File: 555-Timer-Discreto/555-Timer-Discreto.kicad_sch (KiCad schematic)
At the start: 24 parts, among them Q1 2N3904, Q10 2N3906, Q11 2N3904, Q12 2N3904, Q13 2N3906, Q14 2N3904, Q15 2N3904, Q16 2N3904, Q17 2N3904, Q18 2N3904, Q19 2N3906, Q2 2N3904, Q20 2N3906, Q21 2N3906, Q22 2N3904, Q23 2N3904, Q24 2N3904, Q3 2N3904, Q4 2N3904, Q5 2N3906, Q6 2N3906, Q7 2N3906, Q8 2N3906, Q9 2N3906

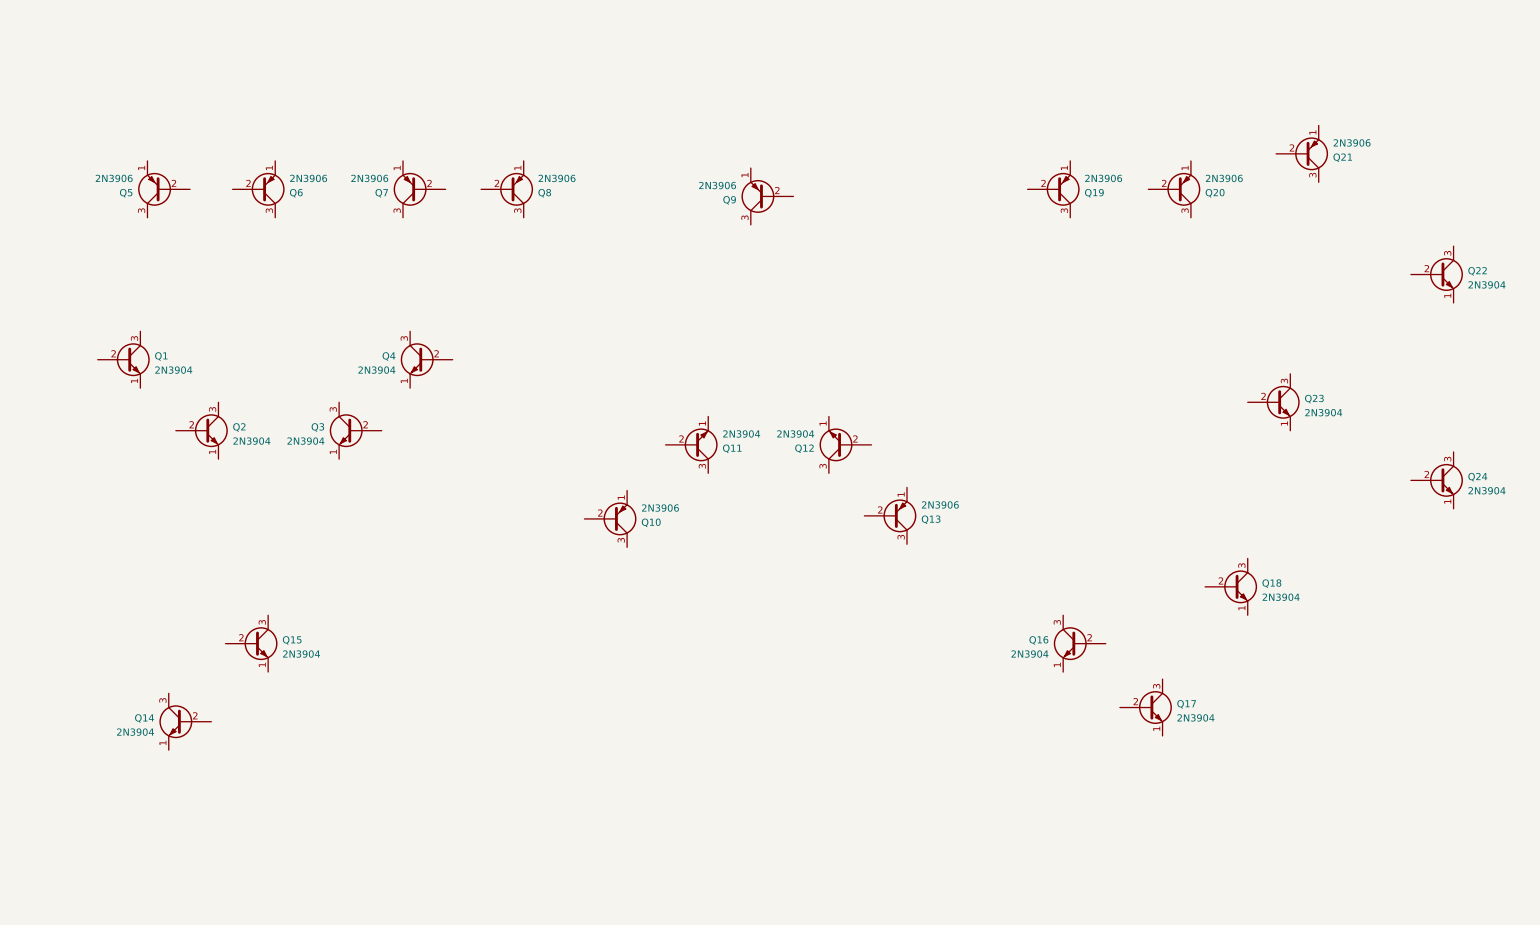
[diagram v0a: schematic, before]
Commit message: Se incorporaron el resto de los componentes y se hicieron las conexiones pertinentes
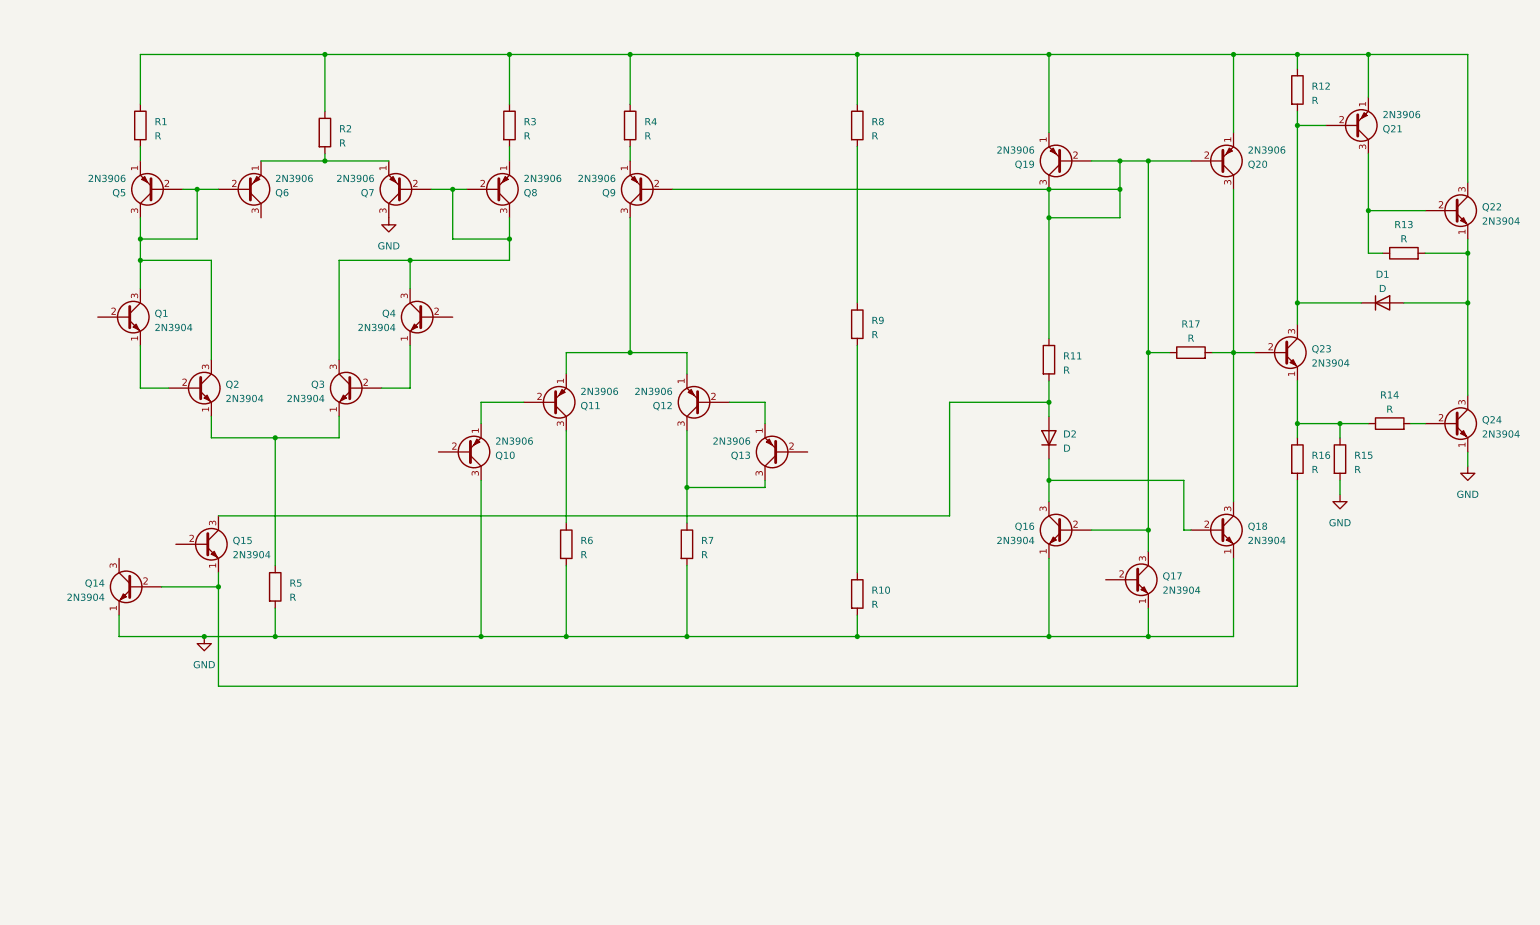
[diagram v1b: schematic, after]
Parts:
- removed Q11, Q12: 2N3904, Package_TO_SOT_THT:TO-92_Inline, symbol Transistor_BJT:2N3904
- added D1, D2: D, symbol Device:D
- added Q11, Q12: 2N3906, Package_TO_SOT_THT:TO-92_Inline, symbol Transistor_BJT:2N3906
- added R1, R10, R11, R12, R13, R14, R15, R16, R17, R2, R3, R4, R5, R6, R7, R8, R9: R, symbol Device:R
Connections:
- net GND: now reaches Q17.1 (E)
- net GND: now also Q10.3 (C), Q14.1 (E), Q16.1 (E), Q18.1 (E), Q24.1 (E), Q7.3 (C), R10.2, R15.2, R5.2, R6.2, R7.2
- net at Q17.3 (C): now also Q16.2 (B), Q19.2 (B), Q19.3 (C), Q20.2 (B), Q9.2 (B), R11.1, R17.1
- net at Q23.1 (E): now also R14.1, R15.1, R16.1
- net at Q23.2 (B): now also Q18.3 (C), Q20.3 (C), R17.2
- net at Q23.3 (C): now also Q21.2 (B), D1.1 (K), R12.2
- net at Q18.2 (B): now also Q16.3 (C), D2.1 (K)
- net at Q15.1 (E): now also Q14.2 (B), R16.2
- net at Q15.3 (C): now also D2.2 (A), R11.2
- net at Q4.1 (E): now also Q3.2 (B)
- net at Q4.3 (C): now also Q3.3 (C), Q7.2 (B), Q8.2 (B), Q8.3 (C)
- net at Q19.1 (E): now also Q20.1 (E), Q21.1 (E), Q22.3 (C), R1.1, R12.1, R2.1, R3.1, R4.1, R8.1
- net at Q10.1 (E): now also Q11.2 (B)
- net at Q9.1 (E): now also R4.2
- net at Q9.3 (C): now also Q11.1 (E), Q12.1 (E)
- net at Q1.1 (E): now also Q2.2 (B)
- net at Q1.3 (C): now also Q2.3 (C), Q5.2 (B), Q5.3 (C), Q6.2 (B)
- net at Q21.3 (C): now also Q22.2 (B), R13.1
- net at Q22.1 (E): now also Q24.3 (C), D1.2 (A), R13.2
- net at Q6.1 (E): now also Q7.1 (E), R2.2
- net at Q5.1 (E): now also R1.2
- net at Q13.1 (E): now also Q12.2 (B)
- net at Q13.3 (C): now also Q12.3 (C), R7.1
- net at Q2.1 (E): now also Q3.1 (E), R5.1
- net at Q8.1 (E): now also R3.2
- net at Q24.2 (B): now also R14.2
- new net: Q11.3 (C), R6.1
- new net: R8.2, R9.1
- new net: R10.1, R9.2
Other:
- title: (none) -> 555 TIMER
- moved on the sheet: Q1, Q10, Q13, Q14, Q15, Q16, Q17, Q18, Q19, Q2, Q20, Q21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

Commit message: Se asignaron huellas a los componentes
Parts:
- D1, D2: footprint (none) -> Diode_THT:D_A-405_P7.62mm_Horizontal
- R1, R10, R11, R12, R13, R14, R15, R16, R17, R2, R3, R4, R5, R6, R7, R8, R9: footprint (none) -> Resistor_THT:R_Axial_DIN0204_L3.6mm_D1.6mm_P5.08mm_Horizontal
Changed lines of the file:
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@@
       (effects (font (size 1.27 1.27)))
     )
-    (property "Footprint" "" (at 255.27 91.948 90)
+    (property "Footprint" "Resistor_THT:R_Axial_DIN0204_L3.6mm_D1.6mm_P5.08mm_Horizontal" (at 255.27 91.948 90)
       (effects (font (size 1.27 1.27)) hide)
     )
@@
       (effects (font (size 1.27 1.27)) (justify left))
     )
-    (property "Footprint" "" (at 127.762 111.76 90)
+    (property "Footprint" "Resistor_THT:R_Axial_DIN0204_L3.6mm_D1.6mm_P5.08mm_Horizontal" (at 127.762 111.76 90)
       (effects (font (size 1.27 1.27)) hide)
     )
@@
       (effects (font (size 1.27 1.27)) (justify left))
     )
-    (property "Footprint" "" (at 29.972 36.83 90)
+    (property "Footprint" "Resistor_THT:R_Axial_DIN0204_L3.6mm_D1.6mm_P5.08mm_Horizontal" (at 29.972 36.83 90)
       (effects (font (size 1.27 1.27)) hide)
     )
@@
       (effects (font (size 1.27 1.27)) (justify left))
     )
-    (property "Footprint" "" (at 106.172 111.76 90)
+    (property "Footprint" "Resistor_THT:R_Axial_DIN0204_L3.6mm_D1.6mm_P5.08mm_Horizontal" (at 106.172 111.76 90)
       (effects (font (size 1.27 1.27)) hide)
     )
@@
       (effects (font (size 1.27 1.27)) (justify left))
     )
-    (property "Footprint" "" (at 244.602 96.52 90)
+    (property "Footprint" "Resistor_THT:R_Axial_DIN0204_L3.6mm_D1.6mm_P5.08mm_Horizontal" (at 244.602 96.52 90)
       (effects (font (size 1.27 1.27)) hide)
     )
@@
       (effects (font (size 1.27 1.27)) (justify left))
     )
-    (property "Footprint" "" (at 96.012 36.83 90)
+    (property "Footprint" "Resistor_THT:R_Axial_DIN0204_L3.6mm_D1.6mm_P5.08mm_Horizontal" (at 96.012 36.83 90)
       (effects (font (size 1.27 1.27)) hide)
     )
@@
       (effects (font (size 1.27 1.27)) (justify left))
     )
-    (property "Footprint" "" (at 158.242 36.83 90)
+    (property "Footprint" "Resistor_THT:R_Axial_DIN0204_L3.6mm_D1.6mm_P5.08mm_Horizontal" (at 158.242 36.83 90)
       (effects (font (size 1.27 1.27)) hide)
     )
@@
       (effects (font (size 1.27 1.27)) (justify left))
     )
-    (property "Footprint" "" (at 236.982 96.52 90)
+    (property "Footprint" "Resistor_THT:R_Axial_DIN0204_L3.6mm_D1.6mm_P5.08mm_Horizontal" (at 236.982 96.52 90)
       (effects (font (size 1.27 1.27)) hide)
     )
@@
       (effects (font (size 1.27 1.27)))
     )
-    (property "Footprint" "" (at 254 68.58 0)
+    (property "Footprint" "Diode_THT:D_A-405_P7.62mm_Horizontal" (at 254 68.58 0)
       (effects (font (size 1.27 1.27)) hide)
     )
@@
       (effects (font (size 1.27 1.27)) (justify left))
     )
-    (property "Footprint" "" (at 236.982 30.48 90)
+    (property "Footprint" "Resistor_THT:R_Axial_DIN0204_L3.6mm_D1.6mm_P5.08mm_Horizontal" (at 236.982 30.48 90)
       (effects (font (size 1.27 1.27)) hide)
     )
@@
       (effects (font (size 1.27 1.27)) (justify left))
     )
-    (property "Footprint" "" (at 62.992 38.1 90)
+    (property "Footprint" "Resistor_THT:R_Axial_DIN0204_L3.6mm_D1.6mm_P5.08mm_Horizontal" (at 62.992 38.1 90)
       (effects (font (size 1.27 1.27)) hide)
     )
@@
       (effects (font (size 1.27 1.27)))
     )
-    (property "Footprint" "" (at 219.71 79.248 90)
+    (property "Footprint" "Resistor_THT:R_Axial_DIN0204_L3.6mm_D1.6mm_P5.08mm_Horizontal" (at 219.71 79.248 90)
       (effects (font (size 1.27 1.27)) hide)
     )
@@
       (effects (font (size 1.27 1.27)) (justify left))
     )
-    (property "Footprint" "" (at 117.602 36.83 90)
+    (property "Footprint" "Resistor_THT:R_Axial_DIN0204_L3.6mm_D1.6mm_P5.08mm_Horizontal" (at 117.602 36.83 90)
       (effects (font (size 1.27 1.27)) hide)
     )
@@
       (effects (font (size 1.27 1.27)) (justify right))
     )
-    (property "Footprint" "" (at 194.31 92.71 0)
+    (property "Footprint" "Diode_THT:D_A-405_P7.62mm_Horizontal" (at 194.31 92.71 0)
       (effects (font (size 1.27 1.27)) hide)
     )
@@
       (effects (font (size 1.27 1.27)) (justify left))
     )
-    (property "Footprint" "" (at 54.102 119.38 90)
+    (property "Footprint" "Resistor_THT:R_Axial_DIN0204_L3.6mm_D1.6mm_P5.08mm_Horizontal" (at 54.102 119.38 90)
       (effects (font (size 1.27 1.27)) hide)
     )
@@
       (effects (font (size 1.27 1.27)))
     )
-    (property "Footprint" "" (at 257.81 61.468 90)
+    (property "Footprint" "Resistor_THT:R_Axial_DIN0204_L3.6mm_D1.6mm_P5.08mm_Horizontal" (at 257.81 61.468 90)
       (effects (font (size 1.27 1.27)) hide)
     )
@@
       (effects (font (size 1.27 1.27)) (justify left))
     )
-    (property "Footprint" "" (at 158.242 72.39 90)
+    (property "Footprint" "Resistor_THT:R_Axial_DIN0204_L3.6mm_D1.6mm_P5.08mm_Horizontal" (at 158.242 72.39 90)
       (effects (font (size 1.27 1.27)) hide)
     )
@@
       (effects (font (size 1.27 1.27)) (justify left))
     )
-    (property "Footprint" "" (at 158.242 120.65 90)
+    (property "Footprint" "Resistor_THT:R_Axial_DIN0204_L3.6mm_D1.6mm_P5.08mm_Horizontal" (at 158.242 120.65 90)
       (effects (font (size 1.27 1.27)) hide)
     )
@@
       (effects (font (size 1.27 1.27)) (justify left))
     )
-    (property "Footprint" "" (at 192.532 78.74 90)
-      (effects (font (size 1.27 1.27)) hide)
-    )
+    (property "Footprint" "Resistor_THT:R_Axial_DIN0204_L3.6mm_D1.6mm_P5.08mm_Horizontal" (at 192.532 78.74 90)
+      (effects (font (size 1.27 1.27)) hide)
+    )

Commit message: Esquemático terminando
Esquemático: se agregaron los conectores y etiquetas de los pines de salida.

PCB: comenzó la organización de los componentes en el espacio físico
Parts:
- added J1, J2: Conn_01x04_Pin, Connector_PinHeader_2.54mm:PinHeader_1x04_P2.54mm_Vertical, symbol Connector:Conn_01x04_Pin
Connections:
- net GND: now also J1.4 (Pin_4)
- net at Q17.2 (B): now also Q11.3 (C), R6.1
- net at Q16.2 (B), Q17.3 (C), Q19.2 (B)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: now also Q6.3 (C)
- net at Q11.1 (E), Q12.1 (E), Q9.3 (C): now also Q4.2 (B)
- net VCC: now reaches Q19.1 (E), Q20.1 (E), Q21.1 (E), Q22.3 (C), R1.1, R12.1, R2.1, R3.1, R4.1, R8.1
- net VCC: now also J2.1 (Pin_1)
- net Reset: now reaches Q15.2 (B)
- net Reset: now also J1.1 (Pin_1)
- net Control Voltage: now reaches R8.2, R9.1
- net Control Voltage: now also J2.4 (Pin_4)
- net Trigger: now reaches Q10.2 (B)
- net Trigger: now also J1.3 (Pin_3)
- net Output: now reaches D1.2 (A), Q22.1 (E), Q24.3 (C), R13.2
- net Output: now also J1.2 (Pin_2)
- net Threshold: now reaches Q1.2 (B)
- net Threshold: now also J2.3 (Pin_3)
- net Discharge: now reaches Q14.3 (C)
- net Discharge: now also J2.2 (Pin_2)
- net at Q13.2 (B): now also R10.1, R9.2
